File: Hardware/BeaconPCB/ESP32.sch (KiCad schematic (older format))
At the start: 13 parts

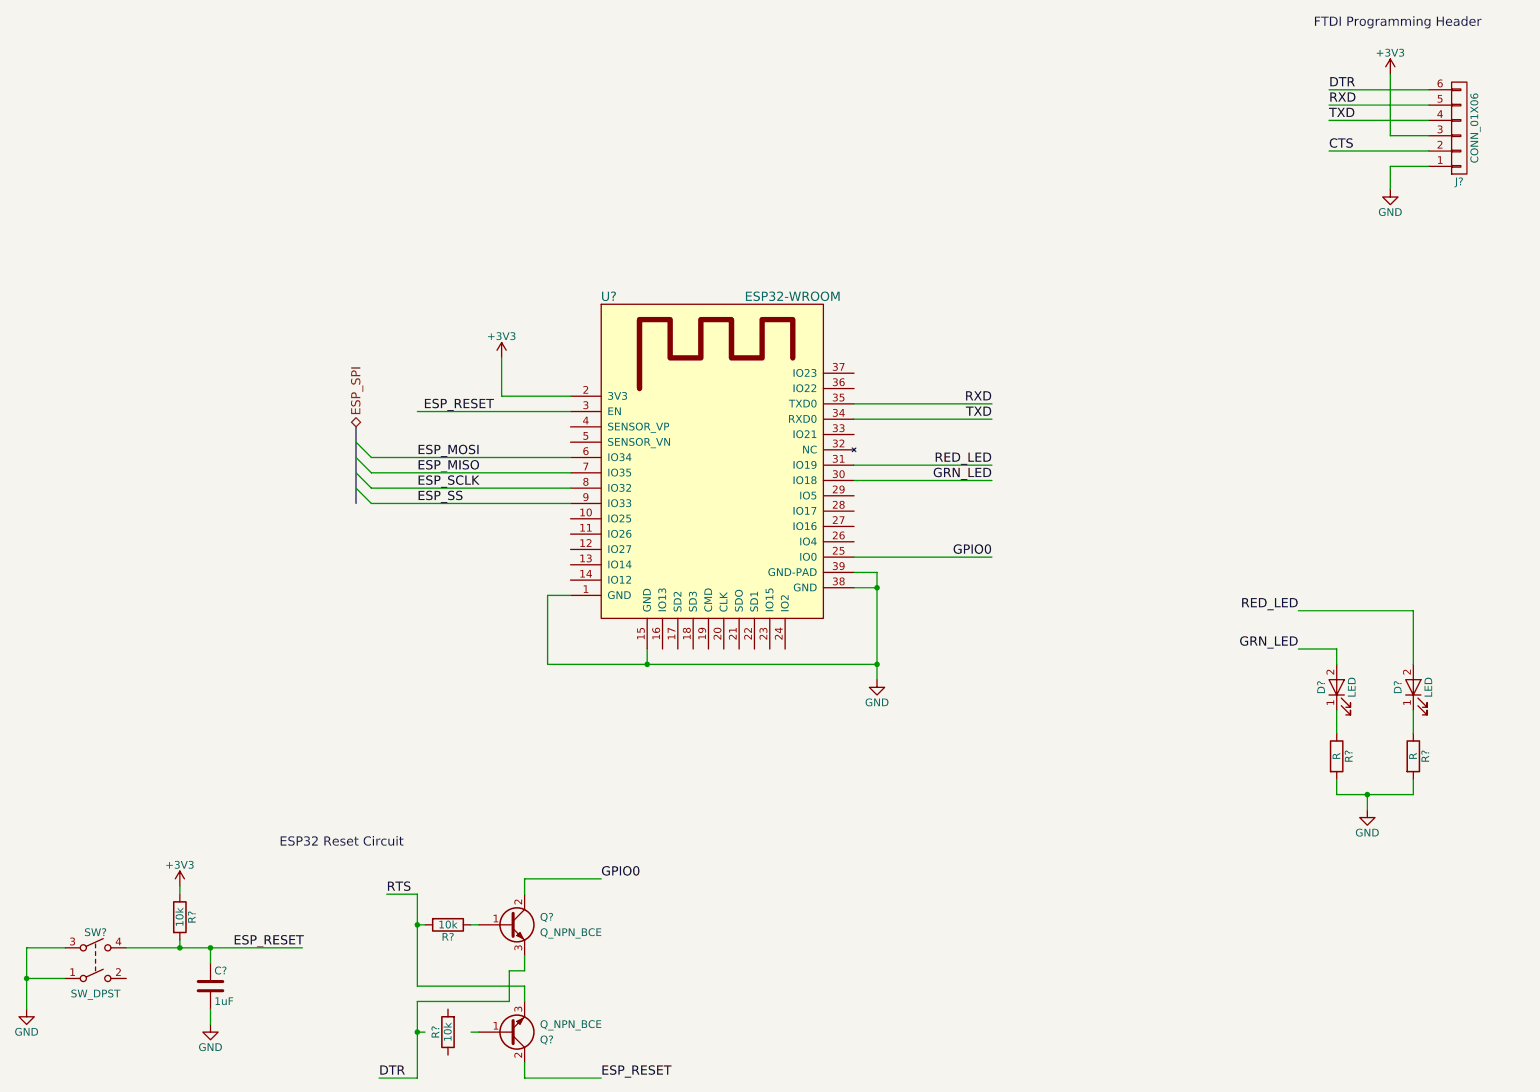
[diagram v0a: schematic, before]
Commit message: Base STM32 circuit schematic done
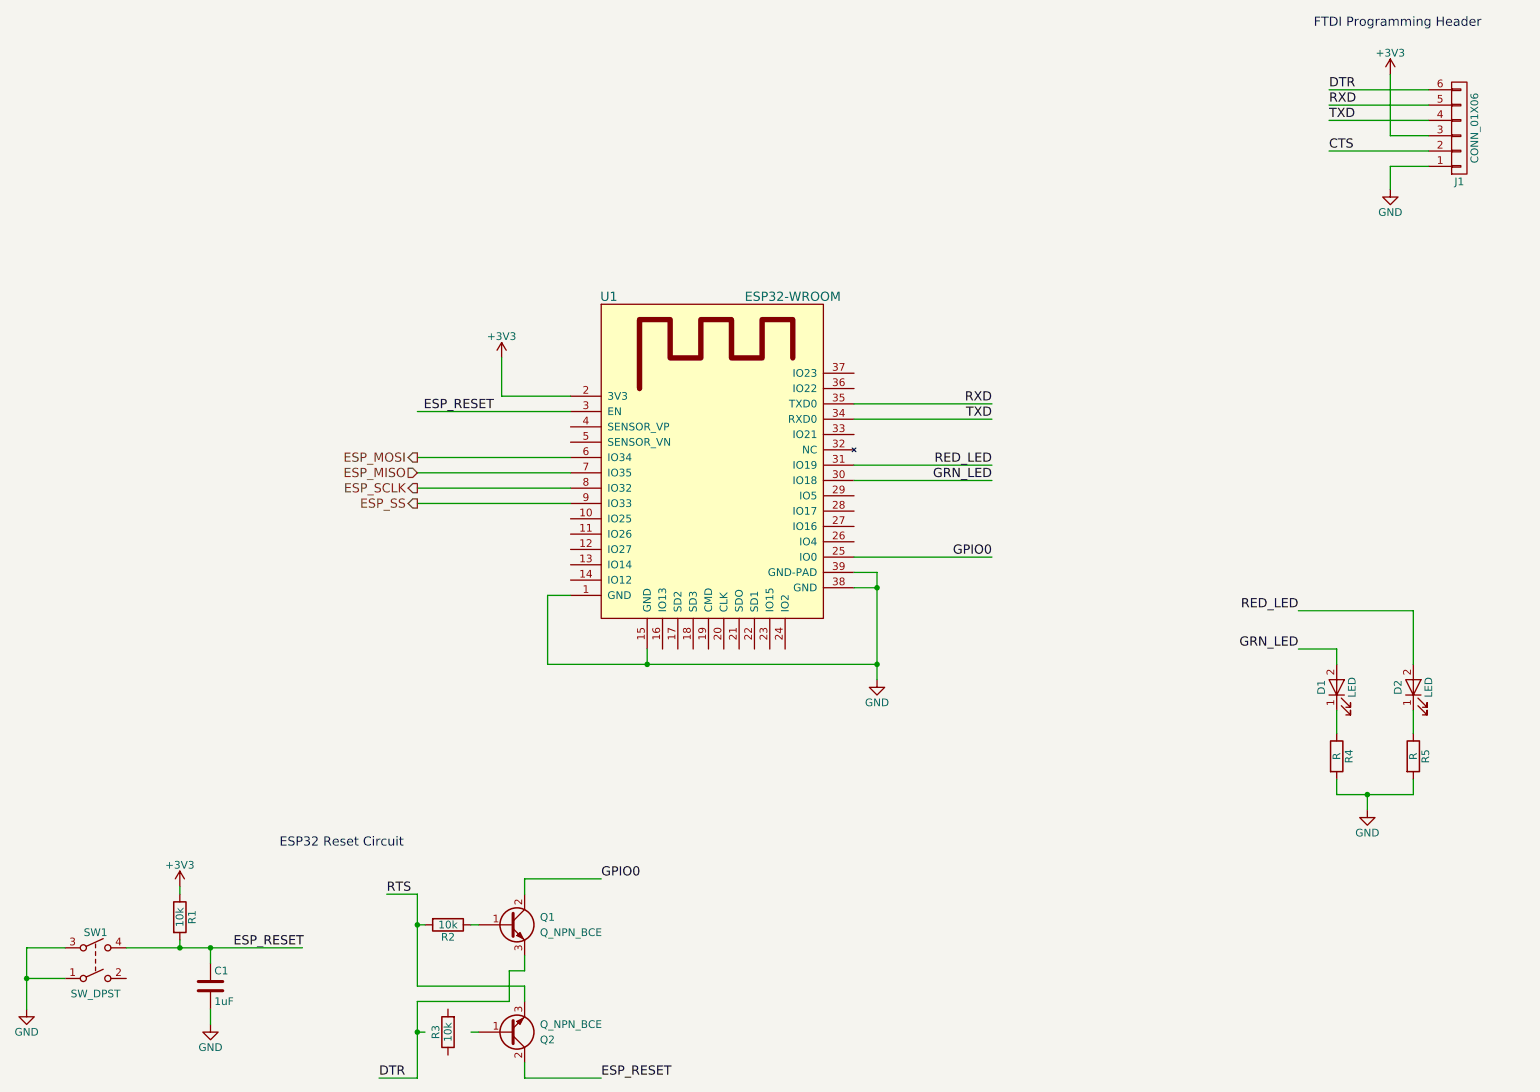
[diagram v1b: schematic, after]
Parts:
- gave numbers to parts that had none: 13
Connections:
- net labels removed: ESP_SPI
- wire segments 63 -> 72
